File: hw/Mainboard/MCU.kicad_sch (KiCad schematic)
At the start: 51 parts, among them J12 NOT_HDMI_A, J13 Micro_SD, J14 USB, J15 DEBUG, SW3 RUN, SW5 BOOTSEL, U14 RP2040, U16 W25Q128JVS, Y1 12 MHz

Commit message: hw: routing (excluding MCU)
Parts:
- removed J14: USB, JLCPCB:MICRO-USB_MICRO-USB-17, symbol Connector:USB_OTG
- added J14: USB_C_Receptacle_USB2.0, JLCPCB:USB-C_SMD-TYPE-C-31-M-12, symbol Connector:USB_C_Receptacle_USB2.0
- added R35, R36: 5k1, Resistor_SMD:R_0402_1005Metric, symbol Device:R_Small
- SW3: footprint SamacSys_Parts:TL4115AF160Q -> JLCPCB:KEY-TH_SKHLLBA010; AliExpress (none) -> https://www.aliexpress.us/item/2251832705063661.html; DIGI-KEY 141-TL4115AF160QCT-ND -> (none); LCSC (none) -> C139765; MOUSER 612-TL4115AF160Q -> (none)
- SW5: footprint Button_Switch_THT:SW_PUSH_6mm -> JLCPCB:SW-TH_L6.0-W3.5-P6.50; Amazon (none) -> https://smile.amazon.com/dp/B008DS188Y; LCSC (none) -> C457531
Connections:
- net GP24 is gone; now on net MCU_CEC: U14.36 (GPIO24)
- net +5V: now also J14.A4 (VBUS), J14.A9 (VBUS), J14.B4 (VBUS), J14.B9 (VBUS), R35.1, R36.1
- net GND: now also J14.A1 (GND), J14.A12 (GND), J14.B1 (GND), J14.B12 (GND), J14.S1 (SHIELD)
- net MCU_CEC: no longer U14.13 (GPIO10)
- net SPI1_SCLK: no longer U14.17 (GPIO14)
- net SPI1_~{READY}: now also U14.13 (GPIO10); no longer U14.14 (GPIO11)
- net USB_D+: now also J14.A6 (D+), J14.B6 (D+)
- net USB_D-: now also J14.A7 (D-), J14.B7 (D-)
- net GP26 renamed ~{CRESET}
- net SPI0_SCLK renamed SPI0_SCK
- new net: J14.A5 (CC1), R35.2
- new net: J14.B5 (CC2), R36.2
- new net MCU_CLK: U14.14 (GPIO11)
- new net SPI1_SCK: U14.17 (GPIO14)
- no-connect marks 3 -> 4

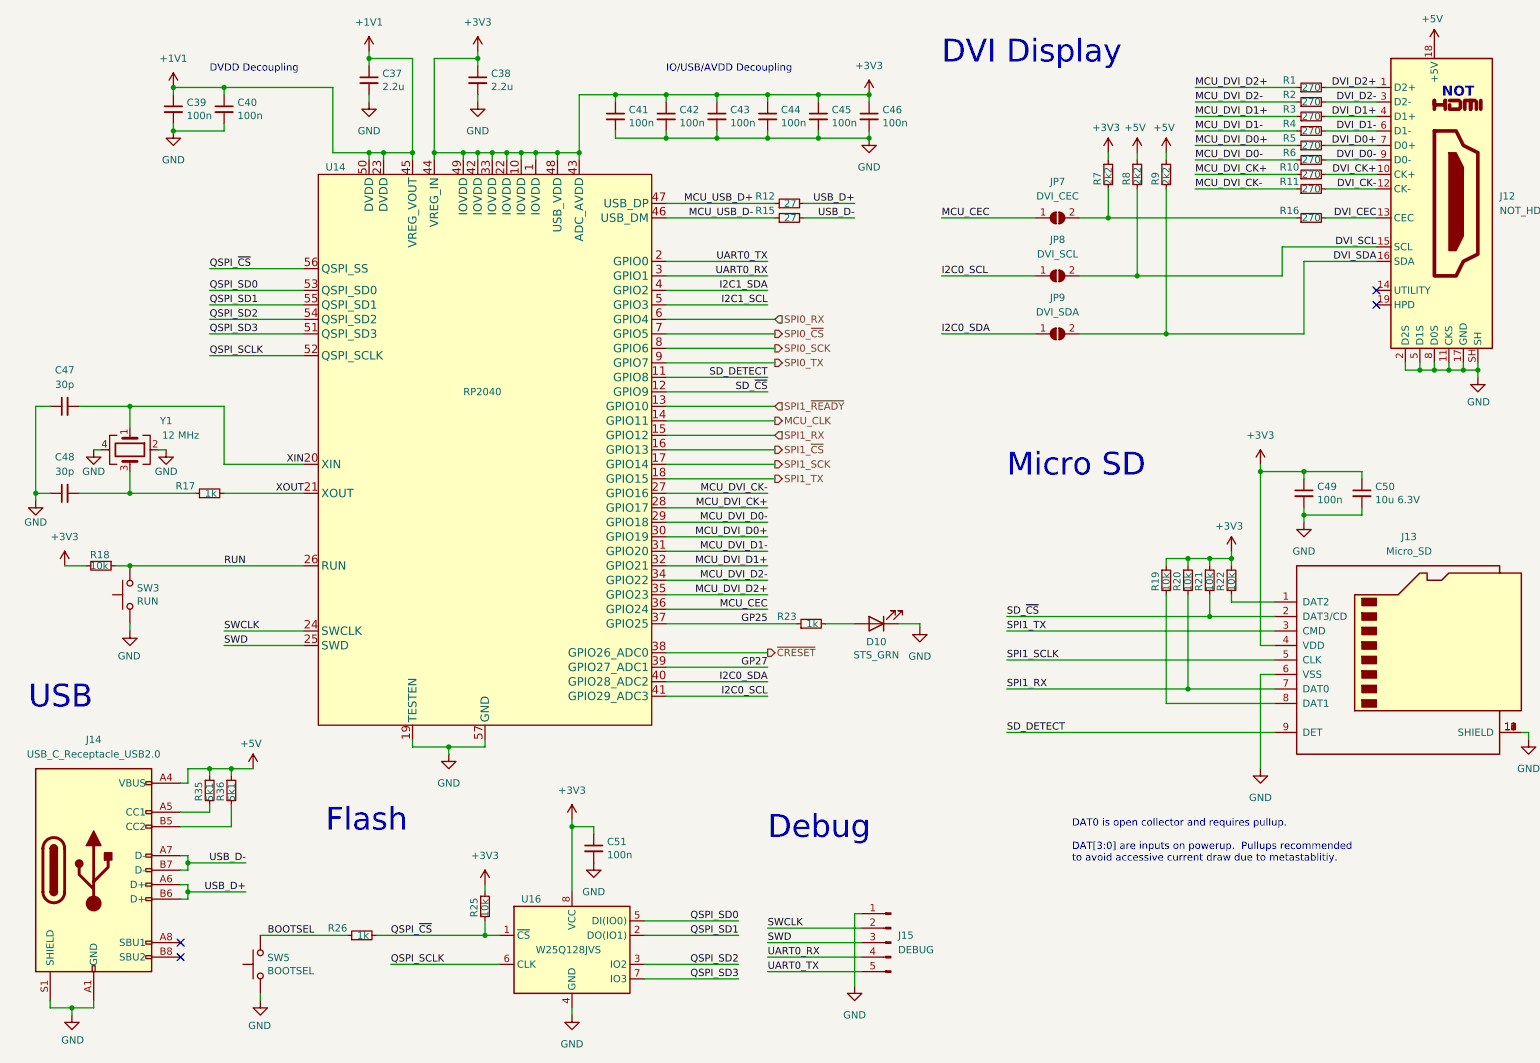
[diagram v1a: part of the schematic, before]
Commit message: hw: routed, but trace sizes need to be reviewed/fixed
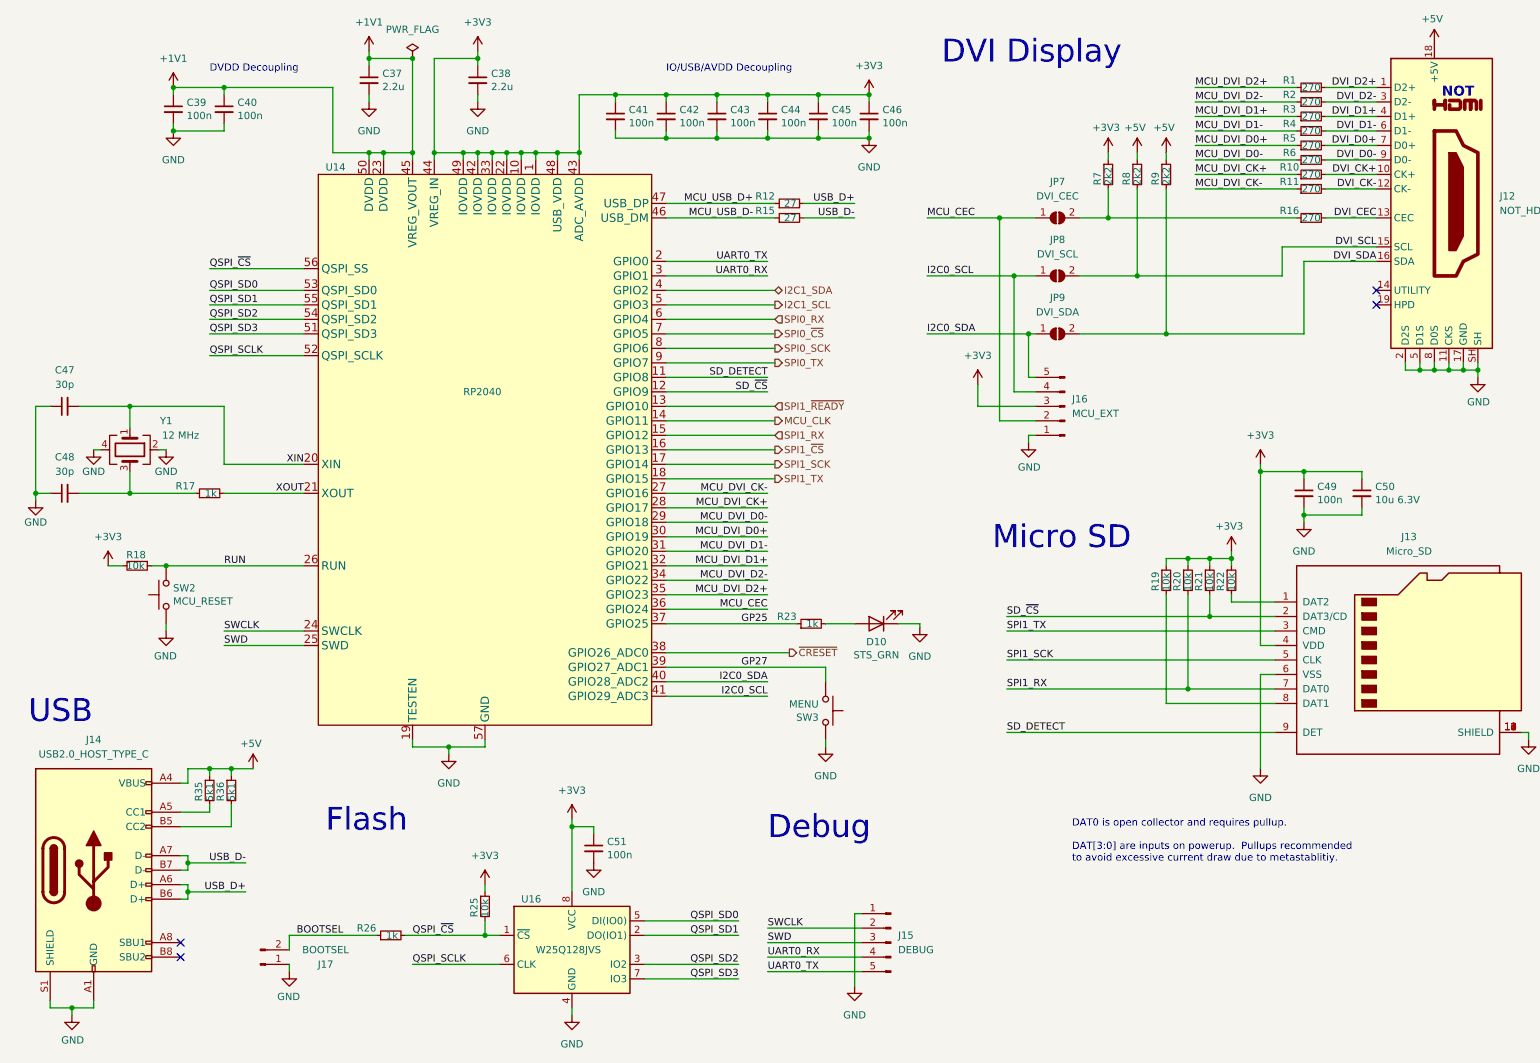
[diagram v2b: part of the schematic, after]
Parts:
- removed SW5: BOOTSEL, JLCPCB:SW-TH_L6.0-W3.5-P6.50, symbol Switch:SW_Push
- added J16: MCU_EXT, Connector_PinHeader_2.54mm:PinHeader_1x05_P2.54mm_Vertical, symbol Connector:Conn_01x05_Male
- added J17: BOOTSEL, Connector_PinHeader_2.54mm:PinHeader_1x02_P2.54mm_Vertical, symbol Connector:Conn_01x02_Male
- added SW2: MCU_RESET, Button_Switch_THT:SW_PUSH_6mm, symbol Switch:SW_Push
- J14: value USB_C_Receptacle_USB2.0 -> USB2.0_HOST_TYPE_C
- SW3: value RUN -> MENU
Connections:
- net SPI1_SCLK is gone; now on net SPI1_SCK: J13.5 (CLK)
- net +3V3: now also J16.3 (Pin_3)
- net BOOTSEL: now also J17.2 (Pin_2)
- net GND: now also SW3.2, J16.1 (Pin_1), J17.1 (Pin_1), SW2.1; no longer SW3.1
- net GP27: now also SW3.1
- net I2C0_SCL: now also J16.4 (Pin_4)
- net I2C0_SDA: now also J16.5 (Pin_5)
- net MCU_CEC: now also J16.2 (Pin_2)
- net RUN: now also SW2.2; no longer SW3.2
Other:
- note added: "DAT0 is open collector and requires pullup. DAT[3:0] are inputs on powerup. Pullups recommended to avoid excessive current draw due to metastablitiy."
- note removed: "DAT0 is open collector and requires pullup. DAT[3:0] are inputs on powerup. Pullups recommended to avoid accessive current draw due to metastablitiy."
- moved on the sheet: R18, R26, SW3

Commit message: hw: routable (wip)
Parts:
- added NT3, NT5: +3V3, PET:NetTie-2_SMD_Pad_0.4_to_0.2mm, symbol Device:NetTie_2
- added NT4: GND, PET:NetTie-2_SMD_Pad_0.4_to_0.2mm, symbol Device:NetTie_2
- added NT6: +5V, PET:NetTie-2_SMD_Pad_0.4_to_0.2mm, symbol Device:NetTie_2
- added R64, R65: 4k7, Resistor_SMD:R_0402_1005Metric, symbol Device:R_Small
- J14: symbol Connector:USB_C_Receptacle_USB2.0 -> JLCPCB:USB_C_Receptacle_USB2.0
- R20: value 10k -> 4k7; LCSC C25744 -> C25900
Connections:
- net +3V3: now also NT3.1, R64.1, R65.1; no longer C38.1, C41.1, C42.1, C43.1, C45.1, C46.1, U14.1 (IOVDD), U14.10 (IOVDD), U14.22 (IOVDD), U14.33 (IOVDD), U14.42 (IOVDD), U14.43 (ADC_AVDD), U14.44 (VREG_IN), U14.48 (USB_VDD), U14.49 (IOVDD)
- net +5V: now also J14.A4_B9 (VBUS), J14.A9_B4 (VBUS), NT6.1; no longer J12.18 (+5V), J14.A4 (VBUS), J14.A9 (VBUS), J14.B4 (VBUS), J14.B9 (VBUS)
- net GND: now also J14.A12_B1 (GND), J14.A1_B12 (GND), NT4.1, NT5.1; no longer J12.11 (CKS), J12.17 (GND), J12.2 (D2S), J12.5 (D1S), J12.8 (D0S), J14.A1 (GND), J14.A12 (GND), J14.B1 (GND), J14.B12 (GND), U14.19 (TESTEN)
- net I2C1_SCL: now also R65.2
- net I2C1_SDA: now also R64.2
- net CC1: now reaches J14.A5 (CC1), R35.2
- net CC2: now reaches J14.B5 (CC2), R36.2
- net +1V1 renamed MCU_DVDD
- new net DVI_GND: J12.11 (CKS), J12.17 (GND), J12.2 (D2S), J12.5 (D1S), J12.8 (D0S), NT4.2
- new net DVI_VDD: J12.18 (+5V), NT6.2
- new net MCU_IOVDD: C38.1, C41.1, C42.1, C43.1, C45.1, C46.1, NT3.2, U14.1 (IOVDD), U14.10 (IOVDD), U14.22 (IOVDD), U14.33 (IOVDD), U14.42 (IOVDD), U14.43 (ADC_AVDD), U14.44 (VREG_IN), U14.48 (USB_VDD), U14.49 (IOVDD)
- new net TESTEN: NT5.2, U14.19 (TESTEN)
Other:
- note added: "DAT0 (RX) is open collector and gets stronger pullup. DAT[3:1] are inputs on powerup and get weaker pullups to avoid excessive current draw due to metastablitiy."
- note removed: "DAT0 is open collector and requires pullup. DAT[3:0] are inputs on powerup. Pullups recommended to avoid excessive current draw due to metastablitiy."
- moved on the sheet: C44, C46, J14

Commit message: hw: wip
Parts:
- added NT18, NT20: +5V, PET:NetTie-2_SMD_Pad_1.6_to_0.4mm, symbol Device:NetTie_2
- added NT19, NT21: GND, PET:NetTie-2_SMD_Pad_1.6_to_0.4mm, symbol Device:NetTie_2
- added R24, R66: 1k, Resistor_SMD:R_0402_1005Metric, symbol Device:R_Small
- R64, R65: value 4k7 -> 2k2; LCSC C25900 -> C25879
- SW2: footprint Button_Switch_THT:SW_PUSH_6mm -> JLCPCB:SW-TH_L6.0-W3.5-P6.50
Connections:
- net +5V: no longer J14.A4_B9 (VBUS), J14.A9_B4 (VBUS), R35.1, R36.1
- net GND: no longer J14.A12_B1 (GND), J14.A1_B12 (GND), J14.S1 (SHIELD)
- net RUN: now also R24.2, R66.2; no longer SW2.2
- new net: J14.A12_B1 (GND), J14.A1_B12 (GND), J14.S1 (SHIELD), NT19.2, NT21.2
- new net: J14.A4_B9 (VBUS), J14.A9_B4 (VBUS), NT18.2, NT20.2, R35.1, R36.1
- new net: R66.1, SW2.2
- new net PD_5V: NT18.1, NT20.1
- new net PD_GND: NT19.1, NT21.1
- new net ~{FPGA_PROG}: R24.1
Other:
- moved on the sheet: R18, SW2

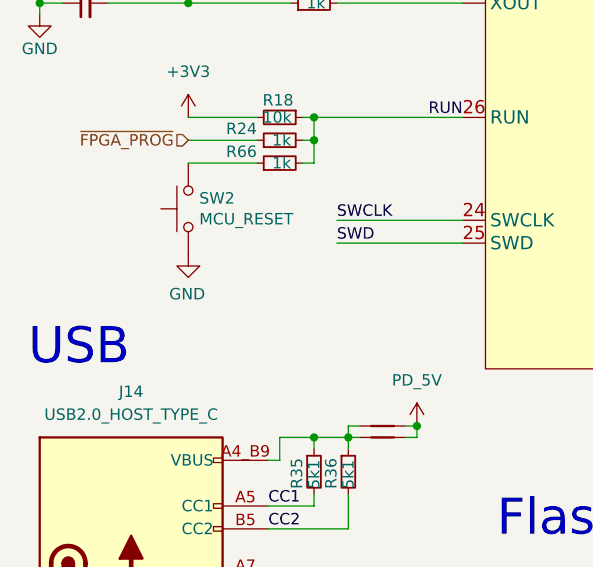
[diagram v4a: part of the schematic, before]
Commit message: hw: pull cbus0 high
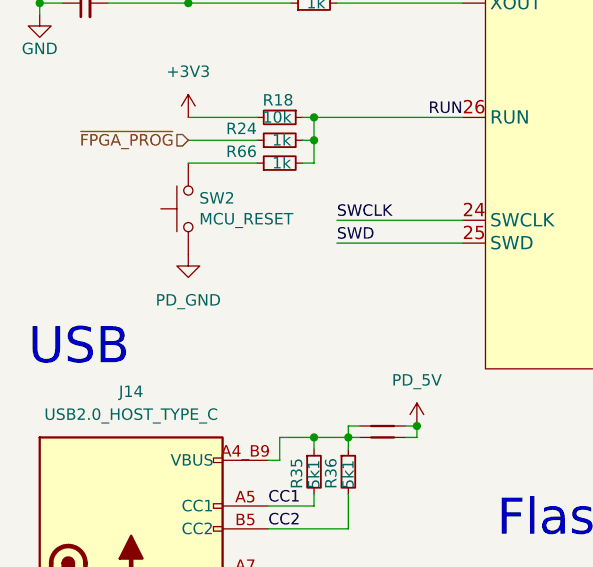
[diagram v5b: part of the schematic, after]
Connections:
- net GND: no longer SW2.1
- net PD_GND: now also SW2.1
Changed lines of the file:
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@@
     (pin "2")
-  )
-  (symbol (lib_id "power:GND") (at 33.02 125.73 0) (mirror y) (unit 1)
-    (in_bom yes) (on_board yes)
-    (property "Reference" "#PWR074" (id 0) (at 33.02 132.08 0)
-      (effects (font (size 1.27 1.27)) hide)
-    )
-    (property "Value" "GND" (id 1) (at 32.893 130.1242 0))
-    (property "Footprint" "" (id 2) (at 33.02 125.73 0)
-      (effects (font (size 1.27 1.27)) hide)
-    )
-    (property "Datasheet" "" (id 3) (at 33.02 125.73 0)
-      (effects (font (size 1.27 1.27)) hide)
-    )
-    (pin "1")
   )
   (symbol (lib_id "Device:R_Small") (at 240.03 41.91 90) (unit 1)
@@
     (pin "9")
   )
+  (symbol (lib_id "PET:PD_GND") (at 33.02 125.73 0) (unit 1)
+    (in_bom yes) (on_board yes) (fields_autoplaced)
+    (property "Reference" "#PWR0177" (id 0) (at 33.02 132.08 0)
+      (effects (font (size 1.27 1.27)) hide)
+    )
+    (property "Value" "PD_GND" (id 1) (at 33.02 130.81 0))
+    (property "Footprint" "" (id 2) (at 33.02 125.73 0)
+      (effects (font (size 1.27 1.27)) hide)
+    )
+    (property "Datasheet" "" (id 3) (at 33.02 125.73 0)
+      (effects (font (size 1.27 1.27)) hide)
+    )
+    (pin "1")
+  )
   (symbol (lib_id "Device:C_Small") (at 118.11 31.75 0) (unit 1)

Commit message: hw: wip
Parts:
- removed J16: MCU_EXT, Connector_PinHeader_2.54mm:PinHeader_1x05_P2.54mm_Vertical, symbol Connector:Conn_01x05_Male
- added J16: MCU, Connector_PinHeader_2.54mm:PinHeader_2x10_P2.54mm_Vertical, symbol Connector_Generic:Conn_02x10_Odd_Even
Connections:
- net +3V3: now also J16.2 (Pin_2)
- net GND: now also J16.1 (Pin_1), J16.20 (Pin_20), J16.7 (Pin_7)
- net I2C0_SCL: now also J16.5 (Pin_5)
- net I2C0_SDA: now also J16.3 (Pin_3)
- net I2C1_SCL: now also J16.6 (Pin_6)
- net I2C1_SDA: now also J16.4 (Pin_4)
- net MCU_CEC: now also J16.8 (Pin_8)
- net MCU_CLK: now also J16.19 (Pin_19)
- net MCU_DVDD: now also J16.17 (Pin_17)
- net SPI0_RX: now also J16.15 (Pin_15)
- net SPI0_SCK: now also J16.11 (Pin_11)
- net SPI0_TX: now also J16.13 (Pin_13)
- net SPI0_~{CS}: now also J16.9 (Pin_9)
- net SPI1_RX: now also J16.12 (Pin_12)
- net SPI1_SCK: now also J16.16 (Pin_16)
- net SPI1_TX: now also J16.18 (Pin_18)
- net SPI1_~{CS}: now also J16.14 (Pin_14)
- net SPI1_~{READY}: now also J16.10 (Pin_10)
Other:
- moved on the sheet: SW3

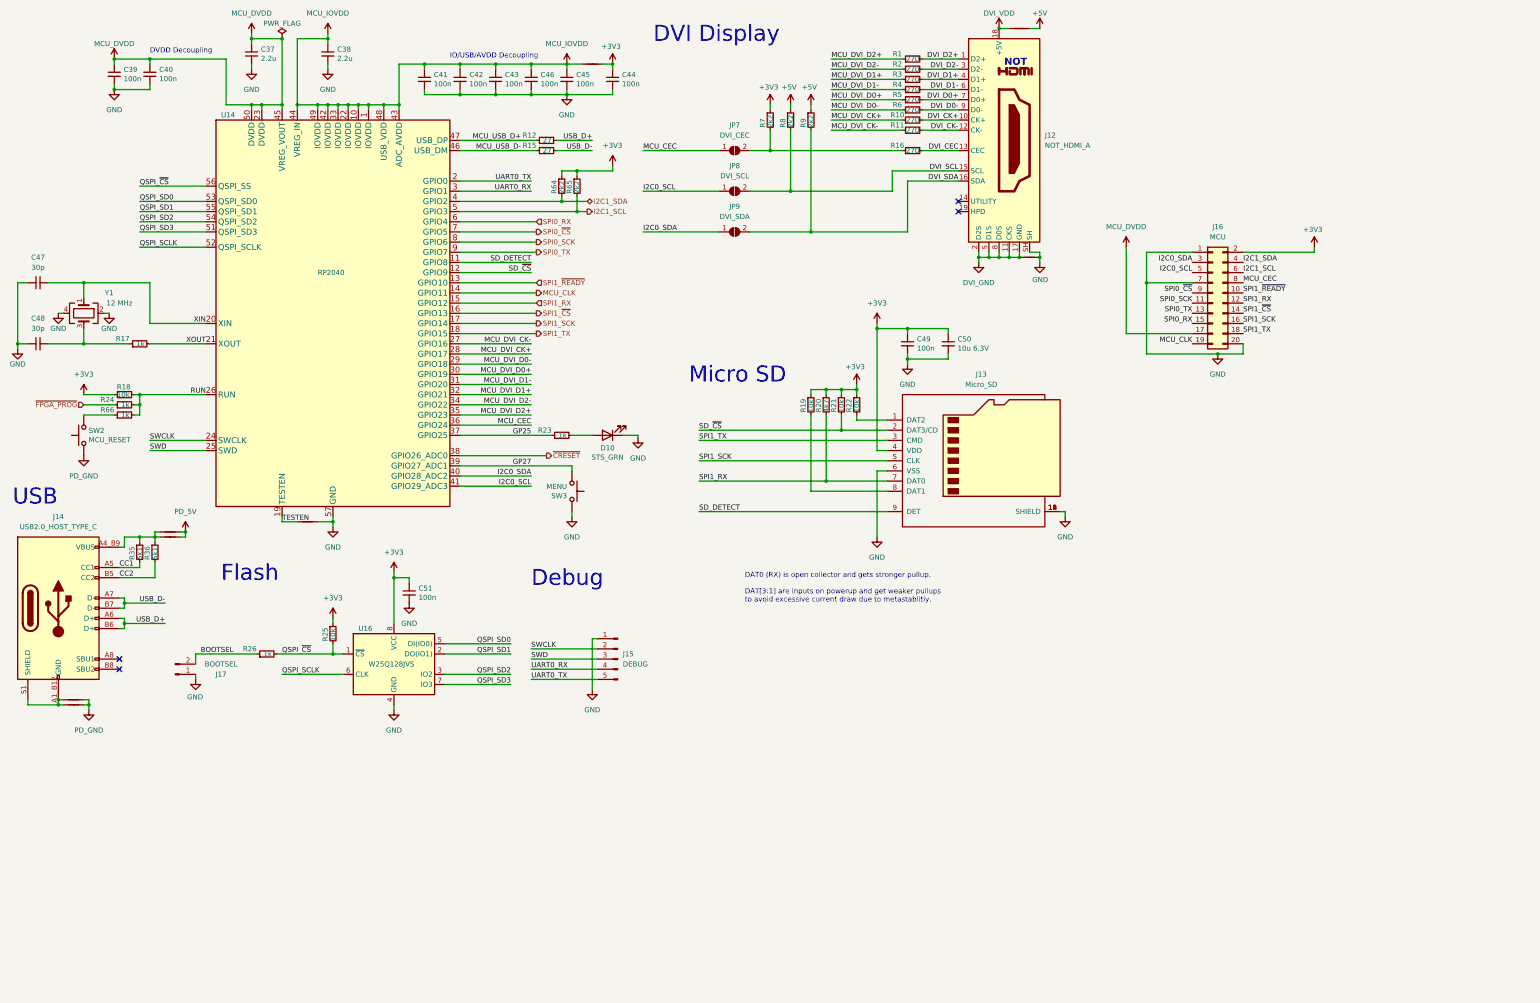
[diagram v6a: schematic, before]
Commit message: hw: larger schematic pages, routed w/netties
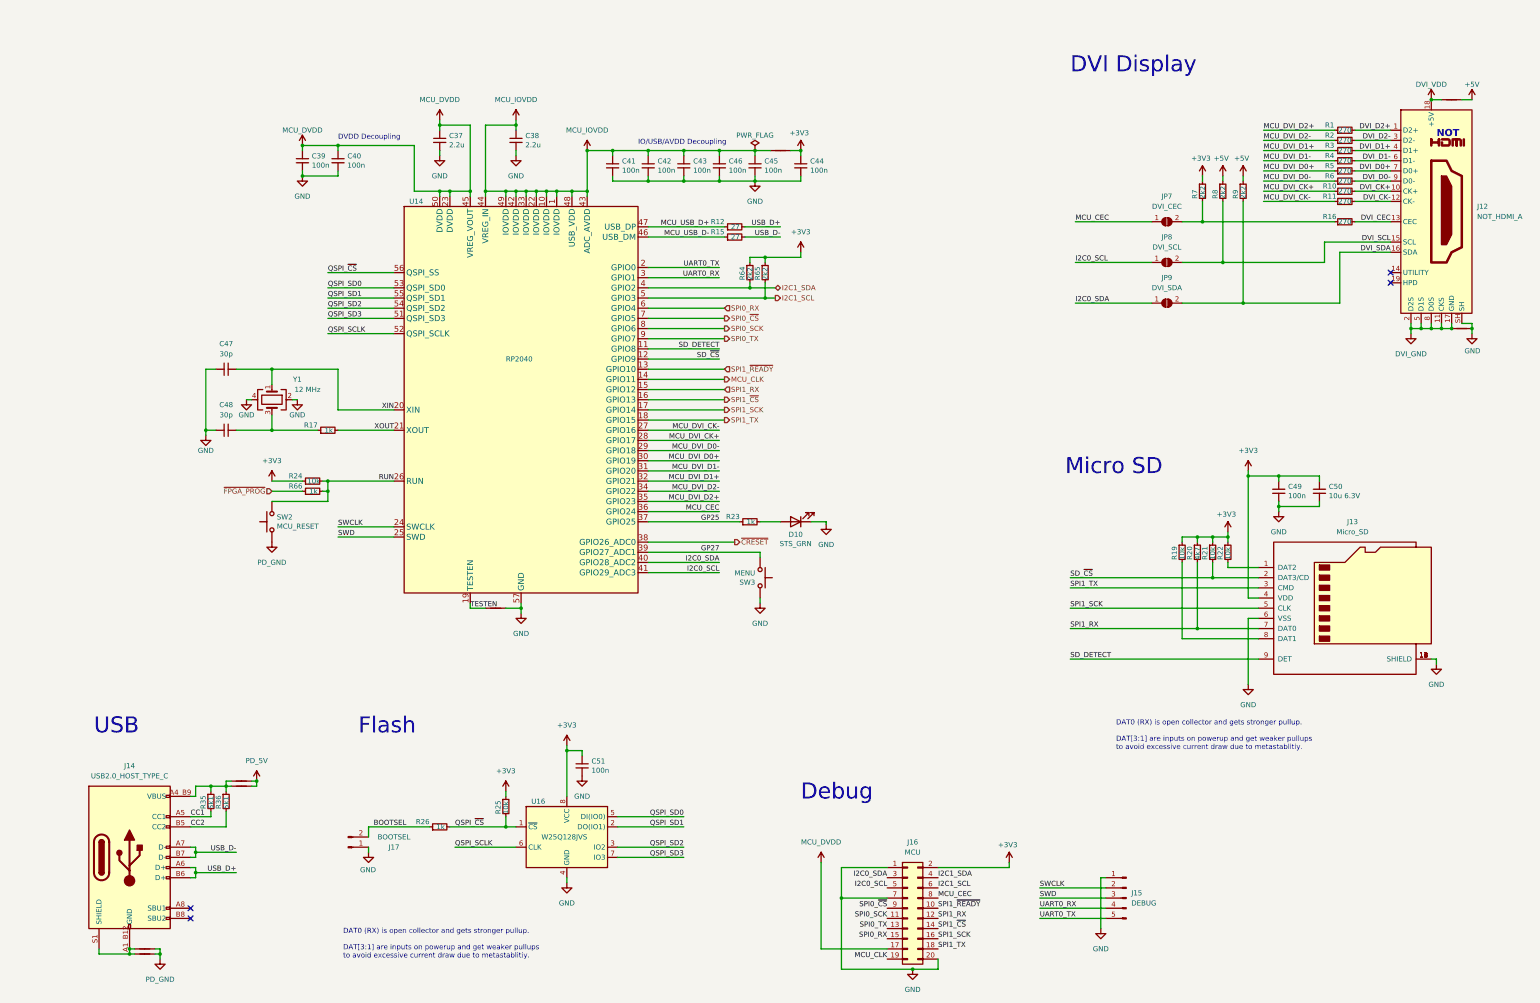
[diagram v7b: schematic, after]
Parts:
- removed R18: 10k, Resistor_SMD:R_0402_1005Metric, symbol Device:R_Small
- R24: value 1k -> 10k; LCSC C11702 -> C25744
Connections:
- net +3V3: now also R24.1
- net RUN: now also SW2.2
- net ~{FPGA_PROG}: now also R66.1; no longer R24.1
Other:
- moved on the sheet: C37, C38, C39, C40, C41, C42, C43, C44, C45, C46, C47, C48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
